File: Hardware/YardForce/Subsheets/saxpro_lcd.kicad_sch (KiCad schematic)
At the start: 24 parts, among them Q1 Q_NPN_BEC

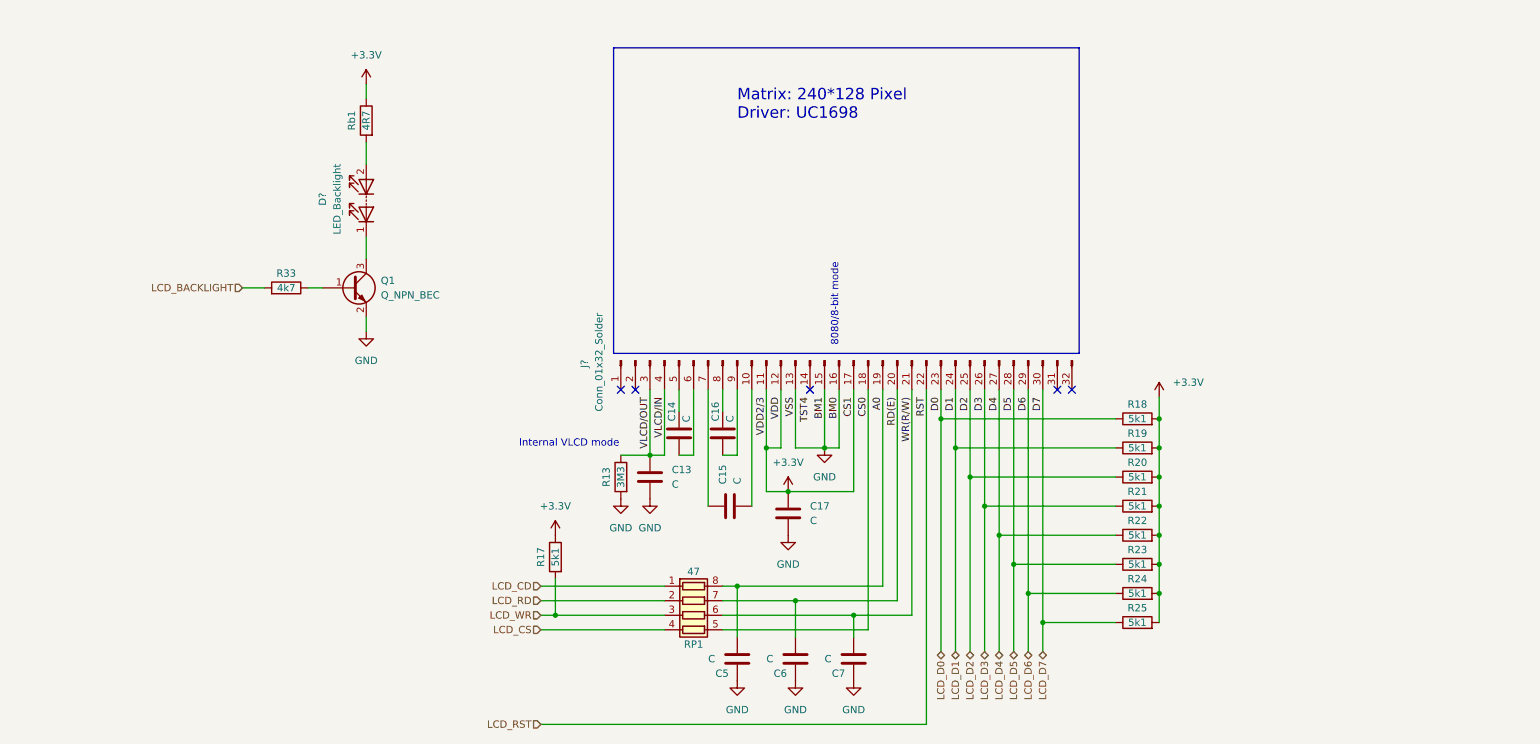
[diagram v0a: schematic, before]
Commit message: Add touch panel
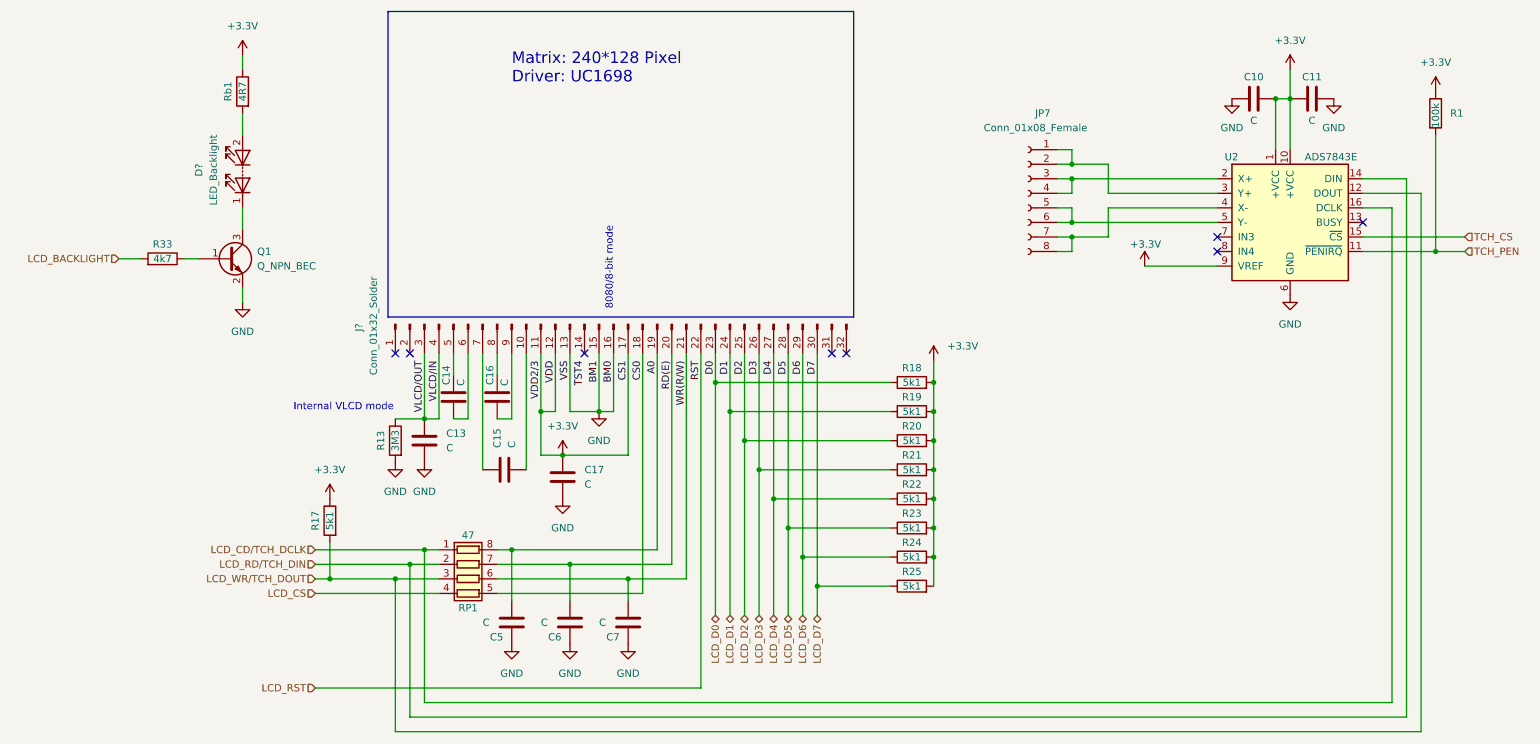
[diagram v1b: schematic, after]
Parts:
- added C10, C11: C, symbol Device:C
- added JP7: Conn_01x08_Female, symbol Connector:Conn_01x08_Female
- added R1: 100k, symbol Device:R
- added U2: ADS7843E, Package_SO:SSOP-16_3.9x4.9mm_P0.635mm, symbol Driver_Display:ADS7843E
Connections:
- net +3.3V: now also C10.1, C11.2, R1.1, U2.1 (+VCC), U2.10 (+VCC), U2.9 (VREF)
- net GND: now also C10.2, C11.1, U2.6 (GND)
- net LCD_CD renamed LCD_CD/TCH_DCLK
- net LCD_CD/TCH_DCLK: now also U2.16 (DCLK)
- net LCD_RD renamed LCD_RD/TCH_DIN
- net LCD_RD/TCH_DIN: now also U2.14 (DIN)
- net LCD_WR renamed LCD_WR/TCH_DOUT
- net LCD_WR/TCH_DOUT: now also U2.12 (DOUT)
- new net: JP7.3 (Pin_3), JP7.4 (Pin_4), U2.2 (X+)
- new net: JP7.1 (Pin_1), JP7.2 (Pin_2), U2.3 (Y+)
- new net: JP7.7 (Pin_7), JP7.8 (Pin_8), U2.4 (X-)
- new net: JP7.5 (Pin_5), JP7.6 (Pin_6), U2.5 (Y-)
- new net TCH_CS: U2.15 (~{CS})
- new net TCH_PEN: R1.2, U2.11 (~{PENIRQ})
- no-connect marks 5 -> 8
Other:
- moved on the sheet: C13, C14, C15, C16, C17, C5, C6, C7, D?, J?, Q1, R13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
